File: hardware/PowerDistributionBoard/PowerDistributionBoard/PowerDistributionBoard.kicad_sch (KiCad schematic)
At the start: 93 parts, among them J1 Battery, J10 ESC2_PWR, J2 FAN 1, J3 FAN 2, J4 FAN 3, J5 FAN 4, J6 Inverter, J7 Control Board, J8 Conn_01x02, J9 ESC1_PWR, K1 J115F11AH12VDCS61.5, K2 J115F11AH12VDCS61.5, Q1 Q_NMOS_GDS, Q2 Q_NPN_EBC, Q3 Q_NMOS_GSD, Q4 Q_NMOS_GSD, Q5 Q_NPN_EBC, Q6 Q_NMOS_GSD, Q7 Q_NMOS_GSD, Q8 Q_NPN_BEC, SW1 SW_SPDT, U1 LT1641-1, U2 MAX6643LBBAEET, U3 MAX6643LBBAEET, U4 MC74HC20ADG, U5 KSTW004A2B41Z, U6 AP2210N-3.3TRG1

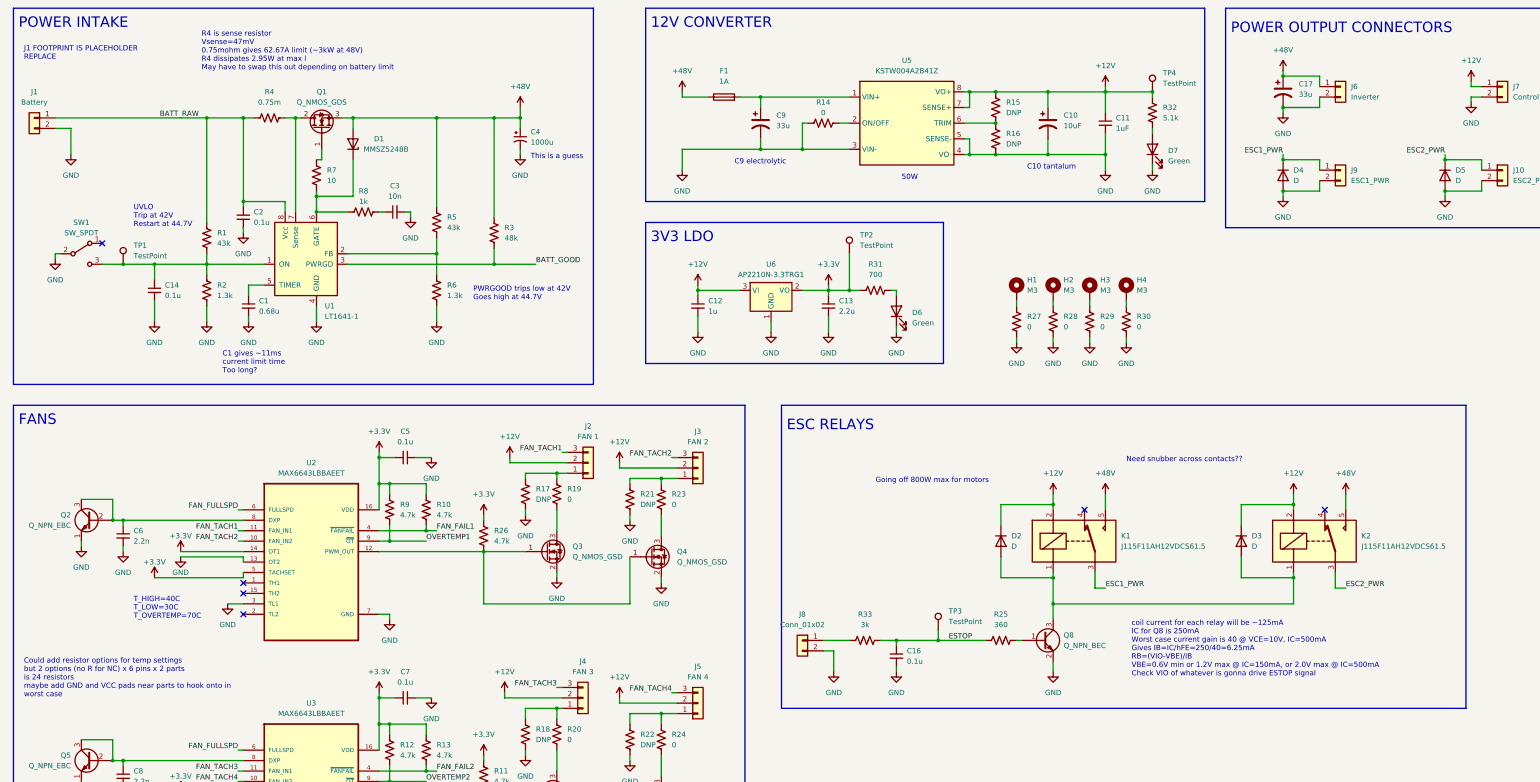
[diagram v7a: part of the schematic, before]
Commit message: Revert "Revert "Pushing current status of control board""
This reverts commit 0a3f5a1237bc2ff3169470f75d528978fa5c2770.
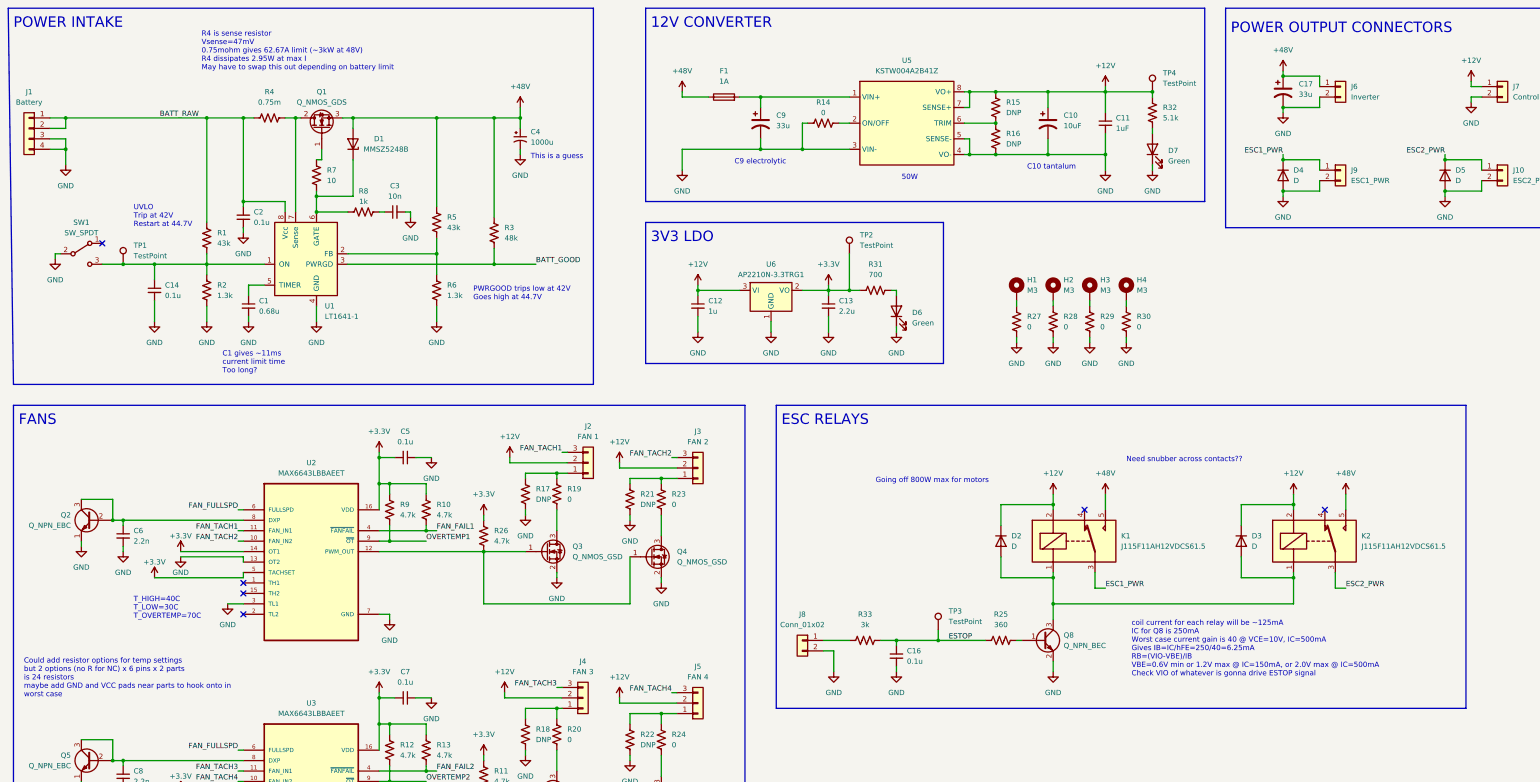
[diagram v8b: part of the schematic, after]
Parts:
- removed J1: Battery, Connector_Molex:Molex_Mini-Fit_Sr_42820-22XX_1x02_P10.00mm_Horizontal, symbol Connector_Generic:Conn_01x02
- added J1: Battery, Connector_Molex:Molex_Mini-Fit_Sr_42820-42XX_1x04_P10.00mm_Horizontal, symbol Connector_Generic:Conn_01x04
- Q1: footprint Package_TO_SOT_SMD:TO-263-3_TabPin2 -> Package_TO_SOT_SMD:TO-263-2; Digikey https://www.digikey.ca/en/products/detail/texas-instruments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 -> 296-49604-1-ND
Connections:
- net BATT_RAW: now also J1.1 (Pin_1), J1.2 (Pin_2)
- net GND: now also J1.3 (Pin_3), J1.4 (Pin_4)
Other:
- note removed: "J1 FOOTPRINT IS PLACEHOLDER REPLACE"
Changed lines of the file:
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@@
   (junction (at 109.22 146.05) (diameter 0) (color 0 0 0 0)
   )
+  (junction (at 30.48 50.8) (diameter 0) (color 0 0 0 0)
+  )
   (junction (at 120.65 43.18) (diameter 0) (color 0 0 0 0)
   )
@@
   (junction (at 100.33 43.18) (diameter 0) (color 0 0 0 0)
   )
+  (junction (at 30.48 43.18) (diameter 0) (color 0 0 0 0)
+  )
   (junction (at 326.39 53.34) (diameter 0) (color 0 0 0 0)
   )
@@
     (stroke (width 0) (type default) (color 0 0 0 0))
   )
-  (polyline (pts (xy 17.78 16.51) (xy 158.75 16.51))
+  (polyline (pts (xy 16.51 16.51) (xy 158.75 16.51))
     (stroke (width 0) (type default) (color 0 0 0 0))
   )
@@
     (stroke (width 0) (type default) (color 0 0 0 0))
   )
-  (wire (pts (xy 27.94 43.18) (xy 64.77 43.18))
+  (wire (pts (xy 26.67 43.18) (xy 30.48 43.18))
     (stroke (width 0) (type default) (color 0 0 0 0))
   )
@@
     (stroke (width 0) (type default) (color 0 0 0 0))
   )
-  (wire (pts (xy 27.94 45.72) (xy 31.75 45.72))
+  (wire (pts (xy 26.67 48.26) (xy 30.48 48.26))
     (stroke (width 0) (type default) (color 0 0 0 0))
   )
@@
     (stroke (width 0) (type default) (color 0 0 0 0))
   )
+  (wire (pts (xy 30.48 45.72) (xy 30.48 43.18))
+    (stroke (width 0) (type default) (color 0 0 0 0))
+  )
   (wire (pts (xy 326.39 60.96) (xy 326.39 62.23))
     (stroke (width 0) (type default) (color 0 0 0 0))
@@
     (stroke (width 0) (type default) (color 0 0 0 0))
   )
+  (wire (pts (xy 26.67 45.72) (xy 30.48 45.72))
+    (stroke (width 0) (type default) (color 0 0 0 0))
+  )
   (wire (pts (xy 250.19 40.64) (xy 250.19 36.83))
     (stroke (width 0) (type default) (color 0 0 0 0))
@@
     (stroke (width 0) (type default) (color 0 0 0 0))
   )
-  (polyline (pts (xy 17.78 16.51) (xy 17.78 107.95))
+  (polyline (pts (xy 16.51 16.51) (xy 17.78 107.95))
     (stroke (width 0) (type default) (color 0 0 0 0))
   )
@@
     (stroke (width 0) (type default) (color 0 0 0 0))
   )
-  (polyline (pts (xy 204.47 113.03) (xy 370.84 113.03))
+  (polyline (pts (xy 203.2 113.03) (xy 370.84 113.03))
     (stroke (width 0) (type default) (color 0 0 0 0))
   )
@@
     (stroke (width 0) (type default) (color 0 0 0 0))
   )
+  (wire (pts (xy 30.48 43.18) (xy 64.77 43.18))
+    (stroke (width 0) (type default) (color 0 0 0 0))
+  )
   (wire (pts (xy 283.21 52.07) (xy 283.21 55.88))
     (stroke (width 0) (type default) (color 0 0 0 0))
@@
     (stroke (width 0) (type default) (color 0 0 0 0))
   )
-  (wire (pts (xy 31.75 45.72) (xy 31.75 52.07))
+  (wire (pts (xy 30.48 48.26) (xy 30.48 50.8))
     (stroke (width 0) (type default) (color 0 0 0 0))
   )
@@
     (stroke (width 0) (type default) (color 0 0 0 0))
   )
-  (polyline (pts (xy 204.47 186.69) (xy 370.84 186.69))
+  (polyline (pts (xy 203.2 186.69) (xy 370.84 186.69))
     (stroke (width 0) (type default) (color 0 0 0 0))
   )
@@
     (stroke (width 0) (type default) (color 0 0 0 0))
   )
+  (wire (pts (xy 30.48 50.8) (xy 30.48 54.61))
+    (stroke (width 0) (type default) (color 0 0 0 0))
+  )
   (wire (pts (xy 106.68 184.15) (xy 106.68 190.5))
     (stroke (width 0) (type default) (color 0 0 0 0))
@@
     (stroke (width 0) (type default) (color 0 0 0 0))
   )
+  (wire (pts (xy 26.67 50.8) (xy 30.48 50.8))
+    (stroke (width 0) (type default) (color 0 0 0 0))
+  )
   (wire (pts (xy 140.97 40.64) (xy 140.97 43.18))
     (stroke (width 0) (type default) (color 0 0 0 0))
@@
     (stroke (width 0) (type default) (color 0 0 0 0))
   )
-  (polyline (pts (xy 204.47 113.03) (xy 204.47 186.69))
+  (polyline (pts (xy 203.2 113.03) (xy 203.2 186.69))
     (stroke (width 0) (type default) (color 0 0 0 0))
   )
@@
     (effects (font (size 1.27 1.27)) (justify left bottom))
   )
-  (text "POWER INTAKE" (at 19.05 21.59 0)
+  (text "POWER INTAKE" (at 17.78 21.59 0)
     (effects (font (size 2.54 2.54)) (justify left bottom))
   )
@@
     (effects (font (size 1.27 1.27)) (justify left bottom))
   )
-  (text "J1 FOOTPRINT IS PLACEHOLDER\nREPLACE" (at 20.32 29.21 0)
-    (effects (font (size 1.27 1.27)) (justify left bottom))
-  )
   (text "Could add resistor options for temp settings\nbut 2 options (no R for NC) x 6 pins x 2 parts\nis 24 resistors\nmaybe add GND and VCC pads near parts to hook onto in\nworst case"
     (at 20.32 184.15 0)
@@
     (effects (font (size 2.54 2.54)) (justify left bottom))
   )
-  (text "ESC RELAYS" (at 205.74 119.38 0)
+  (text "ESC RELAYS" (at 204.47 118.11 0)
     (effects (font (size 2.54 2.54)) (justify left bottom))
   )
@@
     (pin "3")
   )
-  (symbol (lib_id "Connector_Generic:Conn_01x02") (at 22.86 43.18 0) (mirror y) (unit 1)
-    (in_bom yes) (on_board yes) (fields_autoplaced)
-    (property "Reference" "J1" (id 0) (at 22.86 36.83 0))
-    (property "Value" "Battery" (id 1) (at 22.86 39.37 0))
-    (property "Footprint" "Connector_Molex:Molex_Mini-Fit_Sr_42820-22XX_1x02_P10.00mm_Horizontal" (id 2) (at 22.86 43.18 0)
-      (effects (font (size 1.27 1.27)) hide)
-    )
-    (property "Datasheet" "~" (id 3) (at 22.86 43.18 0)
-      (effects (font (size 1.27 1.27)) hide)
-    )
-    (pin "1")
-    (pin "2")
-  )
   (symbol (lib_id "Device:Q_NMOS_GDS") (at 92.71 45.72 90) (unit 1)
     (in_bom yes) (on_board yes)
     (property "Reference" "Q1" (id 0) (at 92.71 36.83 90))
     (property "Value" "Q_NMOS_GDS" (id 1) (at 92.71 39.37 90))
-    (property "Footprint" "Package_TO_SOT_SMD:TO-263-3_TabPin2" (id 2) (at 87.63 48.26 0)
+    (property "Footprint" "Package_TO_SOT_SMD:TO-263-2" (id 2) (at 87.63 48.26 0)
       (effects (font (size 1.27 1.27)) hide)
     )
@@
       (effects (font (size 1.27 1.27)) hide)
     )
-    (property "Digikey" "https://www.digikey.ca/en/products/detail/texas-instruments/CSD19506KTT/5970302" (id 4) (at 92.71 45.72 0)
+    (property "Digikey" "296-49604-1-ND" (id 4) (at 92.71 45.72 0)
       (effects (font (size 1.27 1.27)) hide)
     )
@@
     (pin "1")
   )
+  (symbol (lib_id "Connector_Generic:Conn_01x04") (at 21.59 45.72 0) (mirror y) (unit 1)
+    (in_bom yes) (on_board yes) (fields_autoplaced)
+    (property "Reference" "J1" (id 0) (at 21.59 36.83 0))
+    (property "Value" "Battery" (id 1) (at 21.59 39.37 0))
+    (property "Footprint" "Connector_Molex:Molex_Mini-Fit_Sr_42820-42XX_1x04_P10.00mm_Horizontal" (id 2) (at 21.59 45.72 0)
+      (effects (font (size 1.27 1.27)) hide)
+    )
+    (property "Datasheet" "https://www.molex.com/pdm_docs/sd/428204223_sd.pdf" (id 3) (at 21.59 45.72 0)
+      (effects (font (size 1.27 1.27)) hide)
+    )
+    (property "Digikey" "WM14774-ND" (id 4) (at 21.59 45.72 0)
+      (effects (font (size 1.27 1.27)) hide)
+    )
+    (pin "1")
+    (pin "2")
+    (pin "3")
+    (pin "4")
+  )
   (symbol (lib_id "Device:R_US") (at 149.86 193.04 0) (unit 1)
     (in_bom yes) (on_board yes) (fields_autoplaced)
@@
     (pin "2")
   )
-  (symbol (lib_id "power:GND") (at 31.75 52.07 0) (unit 1)
+  (symbol (lib_id "power:GND") (at 30.48 54.61 0) (unit 1)
     (in_bom yes) (on_board yes) (fields_autoplaced)
-    (property "Reference" "#PWR0117" (id 0) (at 31.75 58.42 0)
+    (property "Reference" "#PWR0117" (id 0) (at 30.48 60.96 0)
       (effects (font (size 1.27 1.27)) hide)
     )
-    (property "Value" "GND" (id 1) (at 31.75 57.15 0))
-    (property "Footprint" "" (id 2) (at 31.75 52.07 0)
+    (property "Value" "GND" (id 1) (at 30.48 59.69 0))
+    (property "Footprint" "" (id 2) (at 30.48 54.61 0)
       (effects (font (size 1.27 1.27)) hide)
     )
-    (property "Datasheet" "" (id 3) (at 31.75 52.07 0)
+    (property "Datasheet" "" (id 3) (at 30.48 54.61 0)
       (effects (font (size 1.27 1.27)) hide)
     )
@@
       (reference "H4") (unit 1) (value "M3") (footprint "MountingHole:MountingHole_3.2mm_M3_Pad_Via")
     )
-    (path "/43aa0335-200f-40da-9db0-d2652ec237fa"
-      (reference "J1") (unit 1) (value "Battery") (footprint "Connector_Molex:Molex_Mini-Fit_Sr_42820-22XX_1x02_P10.00mm_Horizontal")
+    (path "/531994b2-3b90-4304-9bb2-b73527096c79"
+      (reference "J1") (unit 1) (value "Battery") (footprint "Connector_Molex:Molex_Mini-Fit_Sr_42820-42XX_1x04_P10.00mm_Horizontal")
     )
     (path "/47e317a2-b192-4d98-a10e-e011e405dc5c"
@@
     )
     (path "/45186e50-4784-412f-a307-47e14f29fae7"
-      (reference "Q1") (unit 1) (value "Q_NMOS_GDS") (footprint "Package_TO_SOT_SMD:TO-263-3_TabPin2")
+      (reference "Q1") (unit 1) (value "Q_NMOS_GDS") (footprint "Package_TO_SOT_SMD:TO-263-2")
     )
     (path "/310b6666-1d7c-47e0-9c25-bc622b4cd78b"
